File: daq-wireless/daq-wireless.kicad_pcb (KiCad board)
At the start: 2 copper layers, 85 x 85 mm, 4 parts, among them J1 5223002-2, J2 Micro_SD_Card, U1 ESP32-WROOM-32

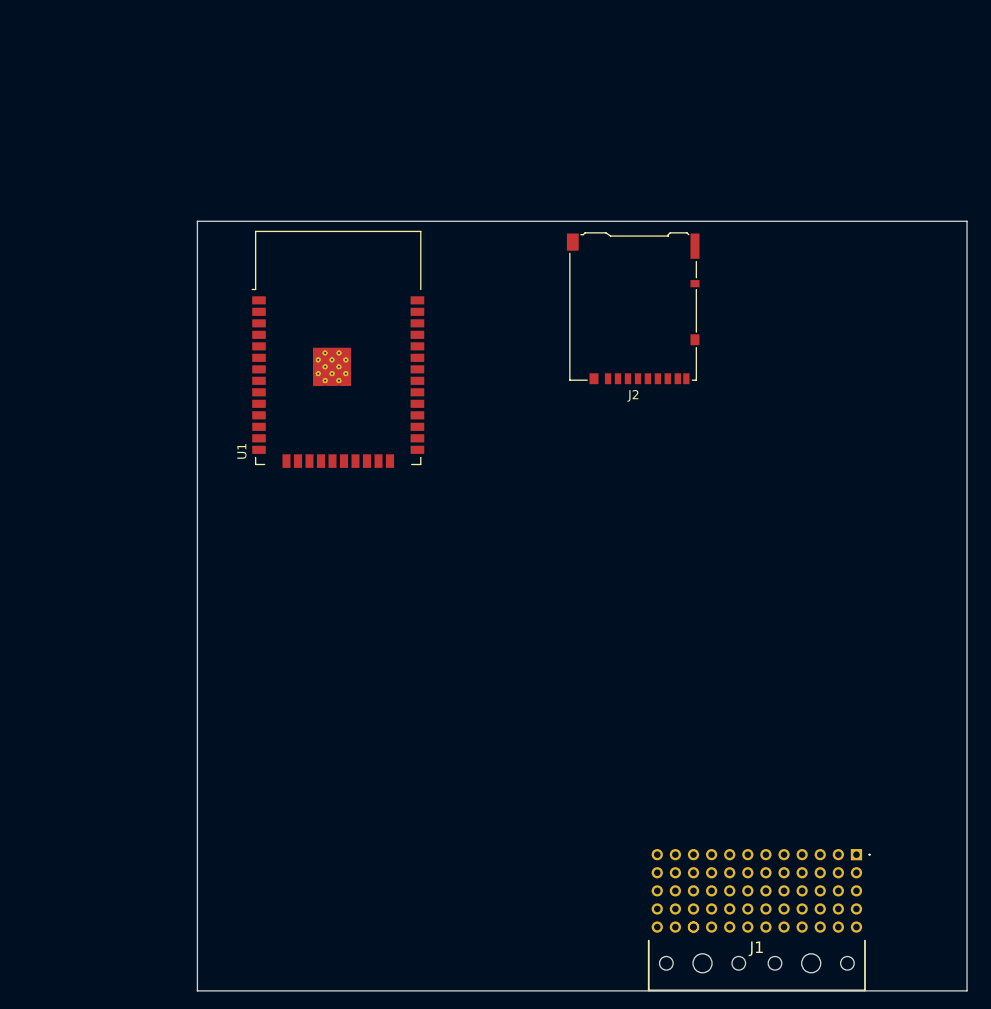
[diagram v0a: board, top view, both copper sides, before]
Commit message: Semiactive, DAQ-wireless updates (schem, board)
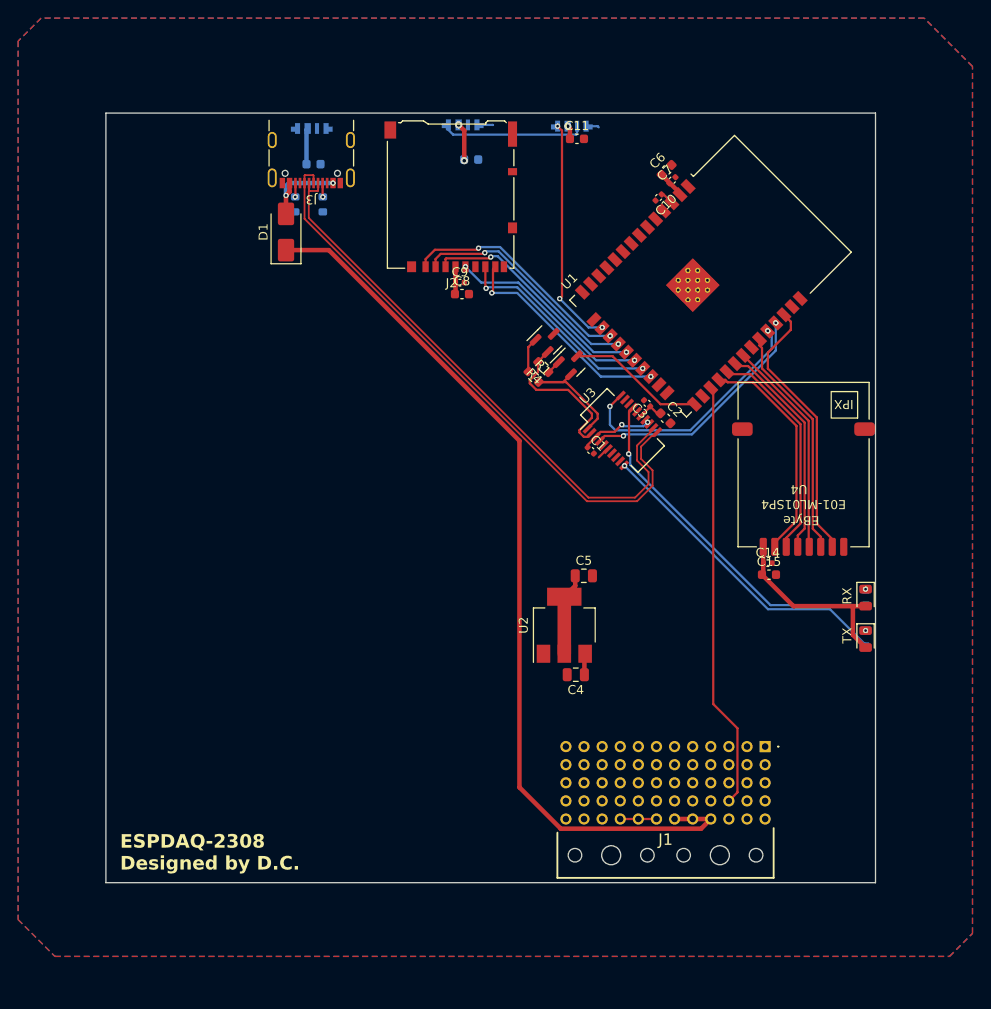
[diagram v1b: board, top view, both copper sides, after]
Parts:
- removed ?: , 
- added C1: .1uF, Capacitor_SMD:C_0402_1005Metric, F.Cu at (145.5, 83.3)
- added C10: .1uF, Capacitor_SMD:C_0402_1005Metric, F.Cu at (153.0, 55.4)
- added C11: 1uF, Capacitor_SMD:C_0603_1608Metric, F.Cu at (144.0, 48.9)
- added C12: 1uF, Capacitor_SMD:C_0603_1608Metric, B.Cu at (132.3, 51.2)
- added C13: 1uF, Capacitor_SMD:C_0603_1608Metric, B.Cu at (114.9, 51.7)
- added C14: .1uF, Capacitor_SMD:C_0402_1005Metric, F.Cu at (165.1, 95.8)
- added C15: 10uF, Capacitor_SMD:C_0603_1608Metric, F.Cu at (165.2, 97.0)
- added C2: 1uF, Capacitor_SMD:C_0603_1608Metric, F.Cu at (153.8, 79.8)
- added C3: .1uF, Capacitor_SMD:C_0402_1005Metric, F.Cu at (151.8, 78.1)
- added C4: 22uF, Capacitor_SMD:C_0805_2012Metric, F.Cu at (143.9, 108.1)
- added C5: 22uF, Capacitor_SMD:C_0805_2012Metric, F.Cu at (144.8, 97.2)
- added C6: 1uF, Capacitor_SMD:C_0603_1608Metric, F.Cu at (153.9, 52.3)
- added C7: .1uF, Capacitor_SMD:C_0402_1005Metric, F.Cu at (154.6, 53.5)
- added C8: 1uF, Capacitor_SMD:C_0603_1608Metric, F.Cu at (131.3, 66.0)
- added C9: .1uF, Capacitor_SMD:C_0402_1005Metric, F.Cu at (131.1, 64.8)
- added D1: D, Diode_SMD:D_SMA, F.Cu at (111.9, 59.2)
- added D2: RX, Diode_SMD:D_0805_2012Metric, F.Cu at (175.9, 99.6)
- added D3: TX, Diode_SMD:D_0805_2012Metric, F.Cu at (175.9, 104.1)
- added D4: STATUS, !footprints:LED_IN-PI42TASPRPGPB, B.Cu at (114.7, 47.6)
- added D7: SD, !footprints:LED_IN-PI42TASPRPGPB, B.Cu at (131.3, 47.2)
- added D9: AUX, !footprints:LED_IN-PI42TASPRPGPB, B.Cu at (143.4, 47.4)
- added J3: USB_C_Receptacle_USB2.0, Connector_USB:USB_C_Receptacle_GCT_USB4105-xx-A_16P_TopMnt_Horizontal, F.Cu at (114.7, 50.1)
- added Q1: MMBT3904, Package_TO_SOT_SMD:SOT-23, F.Cu at (140.8, 71.1)
- added Q2: MMBT3904, Package_TO_SOT_SMD:SOT-23, F.Cu at (143.4, 73.6)
- added R1: 10k, Resistor_SMD:R_0603_1608Metric, F.Cu at (139.2, 75.2)
- added R2: 5.1k, Resistor_SMD:R_0603_1608Metric, B.Cu at (112.9, 56.1)
- added R3: 5.1k, Resistor_SMD:R_0603_1608Metric, B.Cu at (116.0, 56.1)
- added R4: 10k, Resistor_SMD:R_0603_1608Metric, F.Cu at (140.3, 74.1)
- added R5: 1k, Resistor_SMD:R_0603_1608Metric, B.Cu at (175.9, 99.6)
- added R6: 1k, Resistor_SMD:R_0603_1608Metric, B.Cu at (175.9, 104.1)
- added U2: AMS1117, Package_TO_SOT_SMD:SOT-223-3_TabPin2, F.Cu at (142.6, 102.6)
- added U3: FT231XS, Package_SO:SSOP-20_3.9x8.7mm_P0.635mm, F.Cu at (149.0, 81.1)
- added U4: Ebyte_E01-ML01SP4, !footprints:Ebyte E01-ML01SP4, F.Cu at (176.3, 94.0)
- J1: value 5223002-2 -> 5223004-2
- moved U1 40.0 mm to (156.7, 66.2), turned to -45 degrees
- moved J2 23.6 mm to (130.1, 55.3)
- moved J1 15.6 mm to (164.8, 116.0)
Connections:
- J2 pad 4: unconnected-(J2-VDD-Pad4) -> +3V3
- J2 pad 6: unconnected-(J2-VSS-Pad6) -> GND
- J2 pad 9: unconnected-(J2-SHIELD-Pad9) -> GND
- U1 pad 1: Net-(U1-GND-Pad1) -> GND
- U1 pad 15: Net-(U1-GND-Pad1) -> GND
- U1 pad 16: unconnected-(U1-IO13-Pad16) -> /ARGB
- U1 pad 2: unconnected-(U1-VDD-Pad2) -> +3V3
- U1 pad 25: unconnected-(U1-IO0-Pad25) -> /IO0
- U1 pad 27: unconnected-(U1-IO16-Pad27) -> CVT_TX_DAQ_RX
- U1 pad 28: unconnected-(U1-IO17-Pad28) -> /RADIO_CE
- U1 pad 29: unconnected-(U1-IO5-Pad29) -> /RADIO_CS
- U1 pad 3: unconnected-(U1-EN-Pad3) -> /EN
- U1 pad 30: unconnected-(U1-IO18-Pad30) -> /SCK
- U1 pad 31: unconnected-(U1-IO19-Pad31) -> /MOSI
- U1 pad 33: unconnected-(U1-IO21-Pad33) -> /MISO
- U1 pad 34: unconnected-(U1-RXD0/IO3-Pad34) -> /TXD
- U1 pad 35: unconnected-(U1-TXD0/IO1-Pad35) -> /RXD
- U1 pad 36: unconnected-(U1-IO22-Pad36) -> /RADIO_IRQ
- U1 pad 38: Net-(U1-GND-Pad1) -> GND
- U1 pad 39: Net-(U1-GND-Pad1) -> GND
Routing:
- net +5V: track 0.00 -> 114.6 mm, vias 0 -> 3
- net /D+: track 0.00 -> 66.0 mm
- net /D-: track 0.00 -> 64.8 mm
- net CVT_TX_DAQ_RX: track 0.00 -> 46.8 mm
- net Net-(U3-CBUS1): track 0.00 -> 39.0 mm, vias 0 -> 1
- net +3V3: track 0.00 -> 36.1 mm
- net Net-(U3-CBUS2): track 0.00 -> 34.8 mm, vias 0 -> 1
- net /RADIO_IRQ: track 0.00 -> 29.1 mm
- net /TXD: track 0.00 -> 27.7 mm, vias 0 -> 2
- net /RXD: track 0.00 -> 26.6 mm, vias 0 -> 2
- net /SD2: track 0.00 -> 25.8 mm, vias 0 -> 2
- net /SD3: track 0.00 -> 25.6 mm, vias 0 -> 2
- net /ARGB: track 0.00 -> 25.4 mm, vias 0 -> 3
- net /SD_CMD: track 0.00 -> 25.4 mm, vias 0 -> 2
- net /MISO: track 0.00 -> 25.4 mm
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- added copper zone on B.Cu, net GND
- added copper zone on F.Cu, net GND
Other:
- board text added: "ESPDAQ-2308 Designed by D.C."

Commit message: Wireless DAQ  routing
Passes DRC
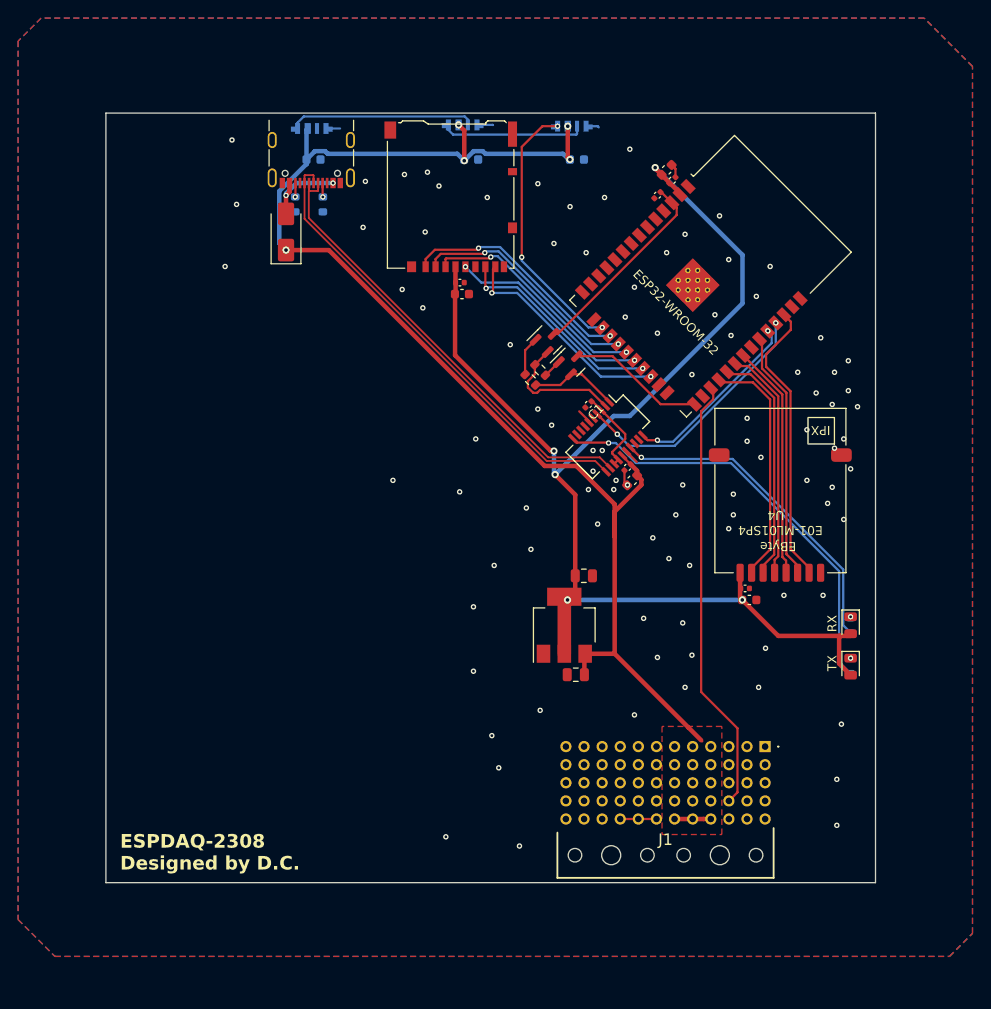
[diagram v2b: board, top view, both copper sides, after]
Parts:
- C11: moved to B.Cu
- moved C2 7.78 mm to (150.1, 86.6), turned to -135 degrees
- moved C3 7.39 mm to (149.6, 85.2), turned to -135 degrees
- moved C1 5.09 mm to (145.3, 78.2), turned to -135 degrees
- moved U4 3.84 mm to (173.7, 96.8)
- moved C14 3.76 mm to (162.6, 98.6)
- moved C15 3.54 mm to (163.1, 99.8)
- moved D2 3.47 mm to (174.2, 102.6)
- moved D3 3.47 mm to (174.2, 107.2)
- moved R5 3.47 mm to (174.2, 102.6)
- moved R6 3.47 mm to (174.2, 107.1)
- moved C11 2.29 mm to (144.0, 51.2)
- moved U3 1.78 mm to (147.4, 81.8), turned to -45 degrees
- moved C13 0.51 mm to (114.9, 51.2)
- moved R1 0.47 mm to (138.9, 75.5)
- moved R4 0.47 mm to (140.0, 74.4)
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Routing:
- net +3V3: track 36.1 -> 141.5 mm, vias 0 -> 5
- net +5V: track 114.6 -> 152.9 mm, vias 3 -> 5
- net /EN: track 1.30 -> 22.3 mm
- net Net-(D4-DIN): track 0.00 -> 20.5 mm
- net /D+: track 66.0 -> 51.5 mm
- net /D-: track 64.8 -> 51.3 mm
- net Net-(U3-CBUS2): track 34.8 -> 47.3 mm
- net /TXD: track 27.7 -> 20.6 mm
- net GND: track 4.53 -> 11.3 mm, vias 0 -> 94
- net /DTR: track 14.0 -> 9.91 mm
- net /ARGB: track 25.4 -> 29.4 mm
- net /RTS: track 16.9 -> 14.0 mm
- net Net-(U3-CBUS1): track 39.0 -> 36.4 mm
- net /RADIO_IRQ: track 29.1 -> 31.3 mm
- net /SCK: track 23.3 -> 25.5 mm
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- added copper zone on F.Cu, net +5V

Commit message: DAQ updates
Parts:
- added G***: LOGO, LOGO, F.Cu at (112.0, 100.6)
- added R7: 10k, Resistor_SMD:R_0603_1608Metric, F.Cu at (151.4, 54.6)
- added SW1: RESET, Button_Switch_THT:SW_PUSH_6mm, F.Cu at (97.4, 48.5)
- moved J2 1.35 mm to (130.1, 56.6)
- moved C9 1.27 mm to (131.1, 66.0)
- moved C8 1.27 mm to (131.3, 67.3)
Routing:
- net /EN: track 22.3 -> 81.2 mm, vias 0 -> 2
- net +3V3: track 141.5 -> 144.1 mm
- net /SD1: track 24.4 -> 23.1 mm
- net /SD0: track 23.5 -> 22.3 mm
- net /SD3: track 25.6 -> 25.0 mm
- net /SD_CMD: track 25.4 -> 24.7 mm
- net /SD_CLK: track 23.0 -> 22.4 mm
- net GND: vias 94 -> 151

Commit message: Critical ESPdaq fix
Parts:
- added R8: 10k, Resistor_SMD:R_0603_1608Metric, F.Cu at (138.8, 65.3)
- added R9: 10k, Resistor_SMD:R_0603_1608Metric, F.Cu at (140.5, 65.3)
- D9: value AUX -> BATT
- moved G*** 2.16 mm to (113.5, 99.1)
- moved C8 1.78 mm to (129.5, 67.3), turned to 180 degrees
- moved C9 1.04 mm to (130.0, 66.0), turned to 180 degrees
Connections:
- U1 pad 10: unconnected-(U1-IO25-Pad10) -> /ARGB
- U1 pad 13: unconnected-(U1-IO14-Pad13) -> /SD_CLK
- U1 pad 14: unconnected-(U1-IO12-Pad14) -> /SD2
- U1 pad 16: /ARGB -> /SD3
- U1 pad 17: /SD2 -> unconnected-(U1-SHD/SD2-Pad17)
- U1 pad 18: /SD3 -> unconnected-(U1-SWP/SD3-Pad18)
- U1 pad 19: /SD_CMD -> unconnected-(U1-SCS/CMD-Pad19)
- U1 pad 20: /SD_CLK -> unconnected-(U1-SCK/CLK-Pad20)
- U1 pad 21: /SD0 -> unconnected-(U1-SDO/SD0-Pad21)
- U1 pad 22: /SD1 -> unconnected-(U1-SDI/SD1-Pad22)
- U1 pad 23: unconnected-(U1-IO15-Pad23) -> /SD_CMD
- U1 pad 24: unconnected-(U1-IO2-Pad24) -> /SD0
- U1 pad 26: unconnected-(U1-IO4-Pad26) -> /SD1
- U1 pad 29: /RADIO_CS -> unconnected-(U1-IO5-Pad29)
- U1 pad 37: unconnected-(U1-IO23-Pad37) -> /RADIO_CS
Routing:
- net /ARGB: track 29.6 -> 17.7 mm, vias 3 -> 1
- net /SD0: track 22.3 -> 33.9 mm
- net +3V3: track 144.1 -> 154.2 mm
- net /RADIO_CS: track 25.0 -> 33.2 mm, vias 0 -> 2
- net /SD2: track 25.4 -> 19.1 mm
- net /SD_CLK: track 22.4 -> 16.6 mm
- net /SD1: track 23.1 -> 28.8 mm
- net /SD_CMD: track 24.7 -> 28.9 mm
- net /SD3: track 25.0 -> 21.2 mm
- net GND: vias 151 -> 175

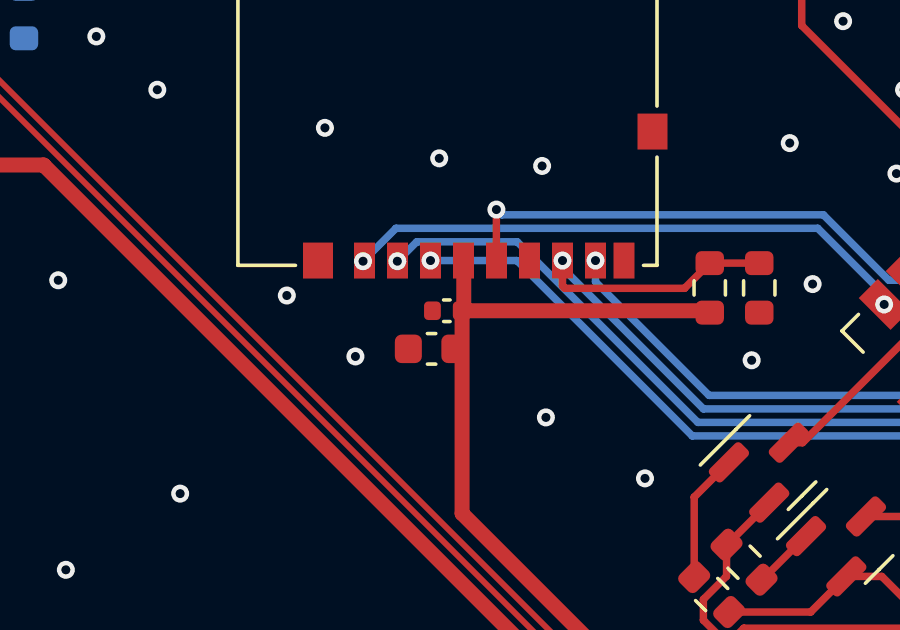
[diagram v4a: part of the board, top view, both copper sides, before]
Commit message: Update SD symbol
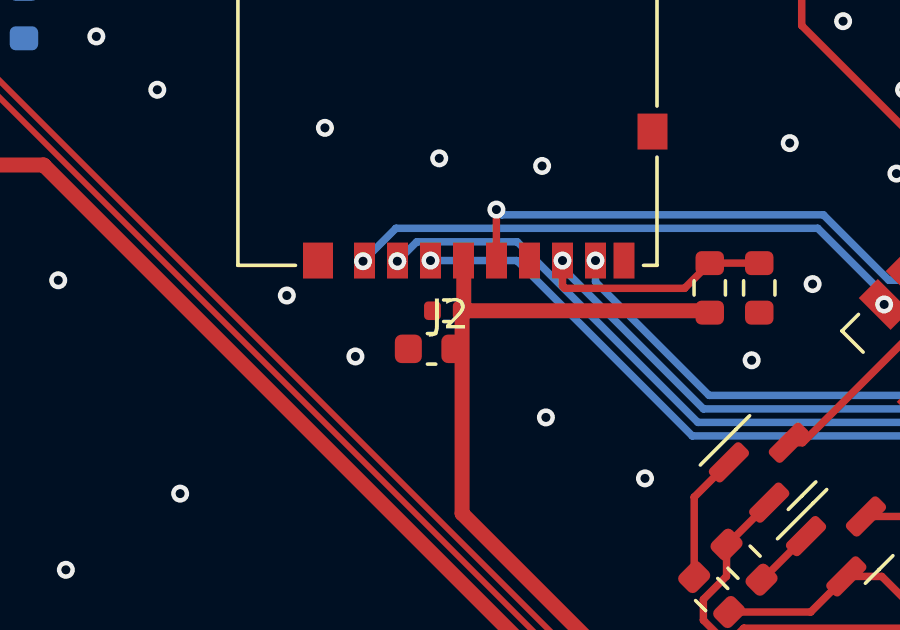
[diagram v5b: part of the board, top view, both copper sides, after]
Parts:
- C10: value .1uF -> 1uF
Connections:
- J2 pad 10: (no net) -> unconnected-(J2-DET_A-Pad10)
- J2 pad 11: (no net) -> GND
- J2 pad 9: GND -> unconnected-(J2-DET_B-Pad9)
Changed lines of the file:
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@@
   (net 112 "unconnected-(U1-SDI{slash}SD1-Pad22)")
   (net 113 "unconnected-(U1-IO5-Pad29)")
+  (net 114 "unconnected-(J2-DET_B-Pad9)")
+  (net 115 "unconnected-(J2-DET_A-Pad10)")
   (footprint "Capacitor_SMD:C_0402_1005Metric" (layer "F.Cu")
     (at 154.559 53.467 45)
@@
         (effects (font (size 1 1) (thickness 0.15)))
     )
-    (fp_text value ".1uF" (at 0 1.16 45) (layer "F.Fab")
+    (fp_text value "1uF" (at 0 1.16 45) (layer "F.Fab")
         (effects (font (size 1 1) (thickness 0.15)))
     )
@@
     (property "Sheetfile" "daq-wireless.kicad_sch")
     (property "Sheetname" "")
-    (property "ki_description" "Micro SD Card Socket")
+    (property "ki_description" "Micro SD Card Socket with card detection pins")
     (property "ki_keywords" "connector SD microsd")
     (attr smd)
-    (fp_text reference "J2" (at -0.075 -9.525) (layer "F.SilkS") hide
+    (fp_text reference "J2" (at -0.075 -9.525 180) (layer "F.SilkS")
         (effects (font (size 1 1) (thickness 0.15)))
     )
-    (fp_text value "Micro_SD_Card" (at -0.075 9.575) (layer "F.Fab")
+    (fp_text value "Micro_SD_Card" (at -0.075 9.575 180) (layer "F.Fab")
         (effects (font (size 1 1) (thickness 0.15)))
     )
-    (fp_text user "KEEPOUT" (at -6.85 -3.25 90) (layer "Cmts.User")
-        (effects (font (size 0.6 0.6) (thickness 0.09)))
+    (fp_text user "KEEPOUT" (at 4.2 7.65 180) (layer "Cmts.User")
+        (effects (font (size 0.4 0.4) (thickness 0.06)))
     )
-    (fp_text user "KEEPOUT" (at -1.075 -1.925) (layer "Cmts.User")
-        (effects (font (size 1 1) (thickness 0.1)))
+    (fp_text user "KEEPOUT" (at -6.85 -3.25 270) (layer "Cmts.User")
+        (effects (font (size 0.6 0.6) (thickness 0.09)))
     )
-    (fp_text user "KEEPOUT" (at -5.775 2.375 90) (layer "Cmts.User")
+    (fp_text user "KEEPOUT" (at -5.775 2.375 270) (layer "Cmts.User")
         (effects (font (size 0.6 0.6) (thickness 0.09)))
     )
-    (fp_text user "KEEPOUT" (at 4.2 7.65) (layer "Cmts.User")
-        (effects (font (size 0.4 0.4) (thickness 0.06)))
+    (fp_text user "KEEPOUT" (at -1.075 -1.925 180) (layer "Cmts.User")
+        (effects (font (size 1 1) (thickness 0.1)))
     )
-    (fp_text user "${REFERENCE}" (at -0.075 0.375) (layer "F.Fab")
+    (fp_text user "${REFERENCE}" (at -0.075 0.375 180) (layer "F.Fab")
         (effects (font (size 1 1) (thickness 0.1)))
     )
@@
       (net 51 "/SD1") (pinfunction "DAT1") (pintype "bidirectional"))
     (pad "9" smd rect (at -5.875 -7.725 180) (size 0.7 1.2) (layers "F.Cu" "F.Paste" "F.Mask")
+      (net 114 "unconnected-(J2-DET_B-Pad9)") (pinfunction "DET_B") (pintype "passive+no_connect"))
+    (pad "10" smd rect (at -6.825 2.775 180) (size 1 0.8) (layers "F.Cu" "F.Paste" "F.Mask")
+      (net 115 "unconnected-(J2-DET_A-Pad10)") (pinfunction "DET_A") (pintype "passive+no_connect"))
+    (pad "11" smd rect (at -6.825 -3.425 180) (size 1 1.2) (layers "F.Cu" "F.Paste" "F.Mask")
+      (net 3 "GND") (pinfunction "SHIELD") (pintype "passive"))
+    (pad "11" smd rect (at -6.825 6.925 180) (size 1 2.8) (layers "F.Cu" "F.Paste" "F.Mask")
+      (net 3 "GND") (pinfunction "SHIELD") (pintype "passive"))
+    (pad "11" smd rect (at 4.325 -7.725 180) (size 1 1.2) (layers "F.Cu" "F.Paste" "F.Mask")
+      (net 3 "GND") (pinfunction "SHIELD") (pintype "passive"))
+    (pad "11" smd rect (at 6.675 7.375 180) (size 1.3 1.9) (layers "F.Cu" "F.Paste" "F.Mask")
       (net 3 "GND") (pinfunction "SHIELD") (pintype "passive"))
-    (pad "10" smd rect (at -6.825 2.775 180) (size 1 0.8) (layers "F.Cu" "F.Paste" "F.Mask"))
-    (pad "11" smd rect (at -6.825 -3.425 180) (size 1 1.2) (layers "F.Cu" "F.Paste" "F.Mask"))
-    (pad "11" smd rect (at -6.825 6.925 180) (size 1 2.8) (layers "F.Cu" "F.Paste" "F.Mask"))
-    (pad "11" smd rect (at 4.325 -7.725 180) (size 1 1.2) (layers "F.Cu" "F.Paste" "F.Mask"))
-    (pad "11" smd rect (at 6.675 7.375 180) (size 1.3 1.9) (layers "F.Cu" "F.Paste" "F.Mask"))
     (zone (net 0) (net_name "") (layer "F.Cu") (hatch full 0.508)
       (connect_pads (clearance 0))
